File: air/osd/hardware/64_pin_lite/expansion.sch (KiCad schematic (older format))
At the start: 2 parts, among them P2 CONN_20, P3 CONN_20

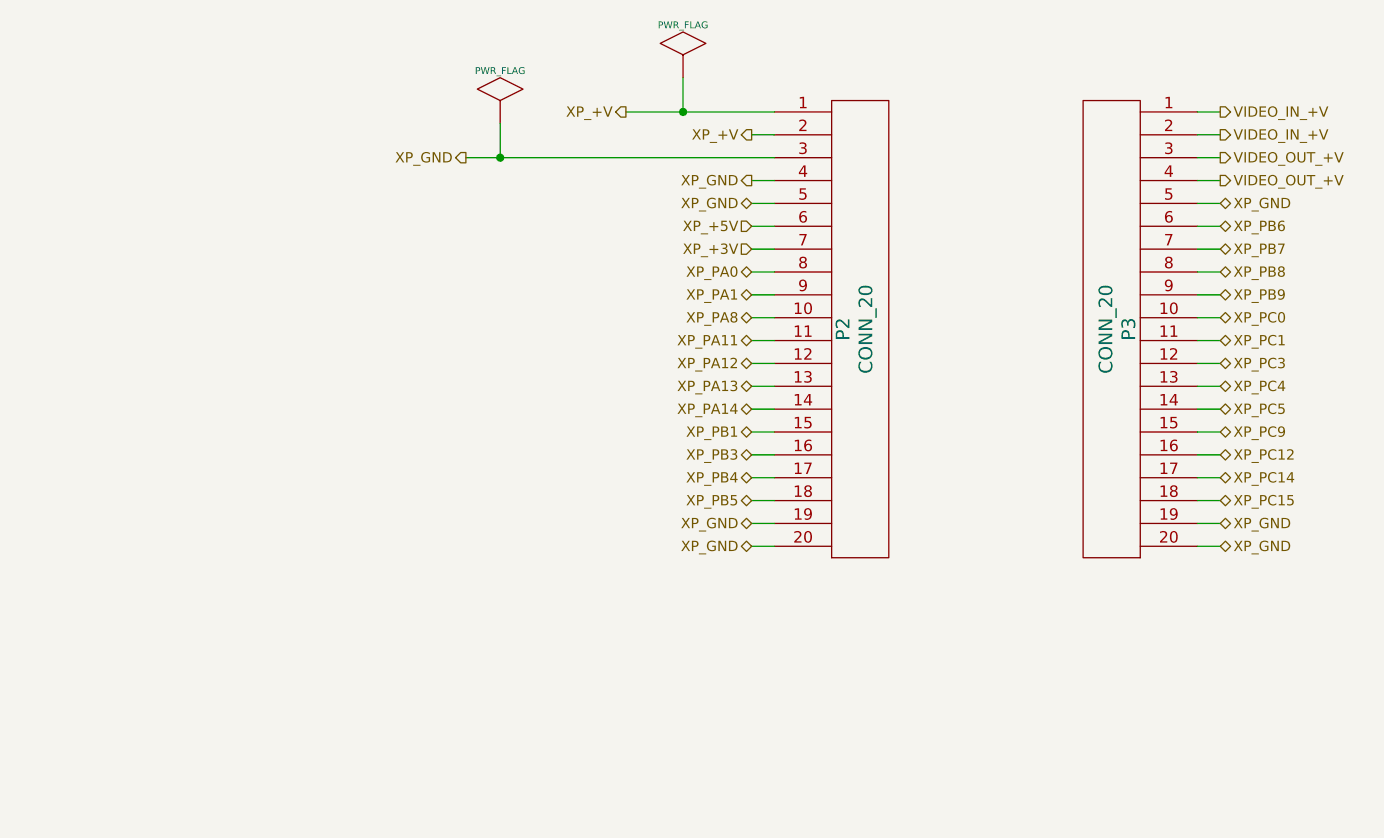
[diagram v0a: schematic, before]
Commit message: osd first  no eror routing of pcb
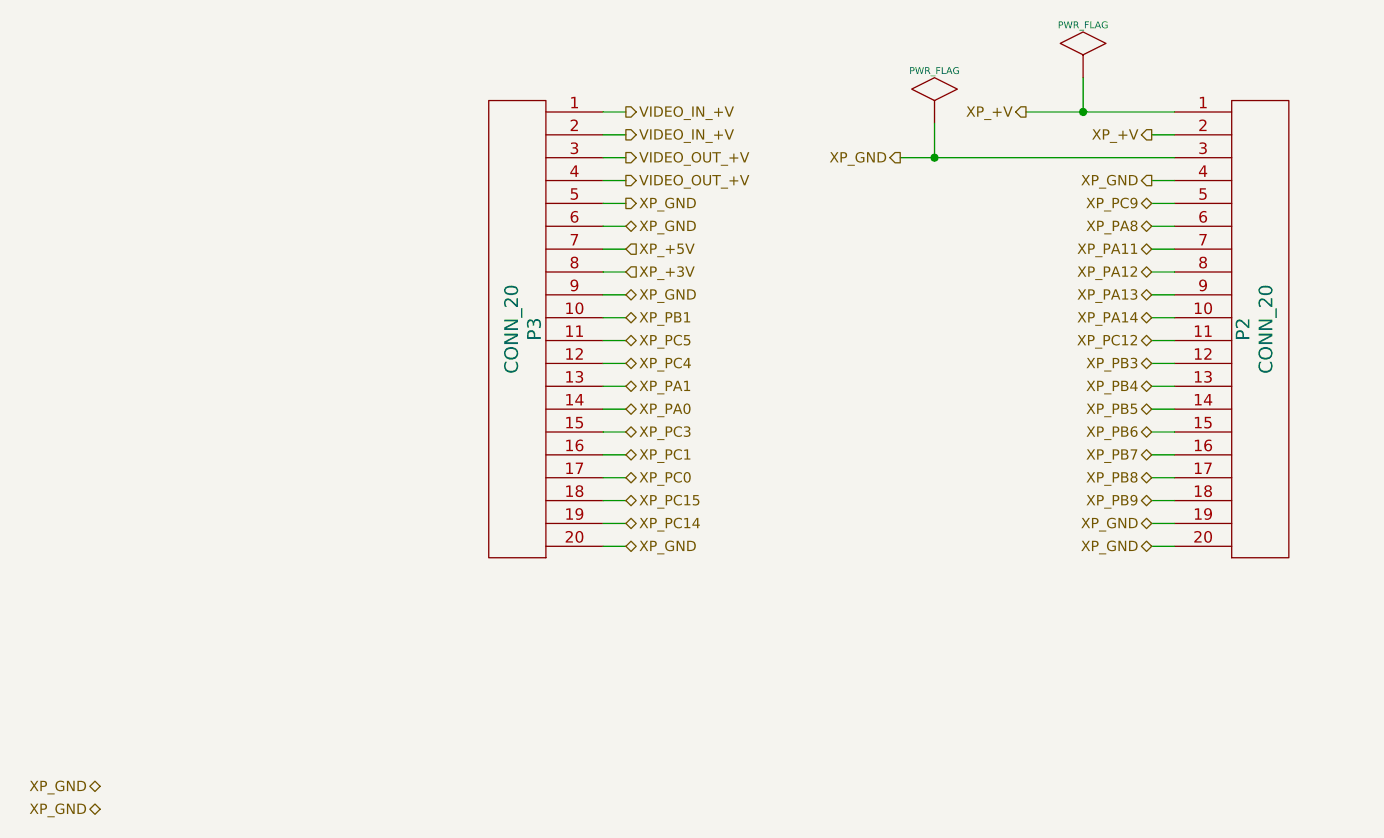
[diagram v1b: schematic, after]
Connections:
- net XP_+3V: now also P3.8 (P8); no longer P2.7 (P7)
- net XP_+5V: now also P3.7 (P7); no longer P2.6 (P6)
- net XP_GND: now also P3.6 (P6), P3.9 (P9); no longer P2.5 (P5), P3.19 (P19)
- net XP_PA0: now also P3.14 (P14); no longer P2.8 (P8)
- net XP_PA1: now also P3.13 (P13); no longer P2.9 (P9)
- net XP_PA11: now also P2.7 (P7); no longer P2.11 (P11)
- net XP_PA12: now also P2.8 (P8); no longer P2.12 (P12)
- net XP_PA13: now also P2.9 (P9); no longer P2.13 (P13)
- net XP_PA14: now also P2.10 (P10); no longer P2.14 (P14)
- net XP_PA8: now also P2.6 (P6); no longer P2.10 (P10)
- net XP_PB1: now also P3.10 (P10); no longer P2.15 (P15)
- net XP_PB3: now also P2.12 (P12); no longer P2.16 (P16)
- net XP_PB4: now also P2.13 (P13); no longer P2.17 (P17)
- net XP_PB5: now also P2.14 (P14); no longer P2.18 (P18)
- net XP_PB6: now also P2.15 (P15); no longer P3.6 (P6)
- net XP_PB7: now also P2.16 (P16); no longer P3.7 (P7)
- net XP_PB8: now also P2.17 (P17); no longer P3.8 (P8)
- net XP_PB9: now also P2.18 (P18); no longer P3.9 (P9)
- net XP_PC0: now also P3.17 (P17); no longer P3.10 (P10)
- net XP_PC1: now also P3.16 (P16); no longer P3.11 (P11)
- net XP_PC12: now also P2.11 (P11); no longer P3.16 (P16)
- net XP_PC14: now also P3.19 (P19); no longer P3.17 (P17)
- net XP_PC3: now also P3.15 (P15); no longer P3.12 (P12)
- net XP_PC4: now also P3.12 (P12); no longer P3.13 (P13)
- net XP_PC5: now also P3.11 (P11); no longer P3.14 (P14)
- net XP_PC9: now also P2.5 (P5); no longer P3.15 (P15)
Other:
- moved on the sheet: P2, P3
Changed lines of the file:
@@
-EESchema Schematic File Version 2  date Thu 27 Nov 2014 15:59:43 GMT
+EESchema Schematic File Version 2  date Sat 29 Nov 2014 10:43:44 GMT
 LIBS:power
 LIBS:device
@@
 Sheet 5 8
 Title ""
-Date "27 nov 2014"
+Date "29 nov 2014"
 Rev ""
 Comp ""
@@
 Comment4 ""
 $EndDescr
-Connection ~ 3650 2700
-Wire Wire Line
-	3650 2550 3650 2700
-Wire Wire Line
-	6700 2800 6800 2800
-Wire Wire Line
-	6700 2600 6800 2600
-Wire Wire Line
-	4200 2500 4850 2500
-Wire Wire Line
-	4850 2700 3500 2700
-Wire Wire Line
-	6800 4300 6700 4300
-Wire Wire Line
-	6700 4400 6800 4400
-Wire Wire Line
-	6700 4100 6800 4100
-Wire Wire Line
-	6700 3900 6800 3900
-Wire Wire Line
-	6700 3700 6800 3700
-Wire Wire Line
-	6700 3500 6800 3500
-Wire Wire Line
-	6700 3300 6800 3300
-Wire Wire Line
-	6700 3100 6800 3100
-Wire Wire Line
-	4850 4400 4750 4400
-Wire Wire Line
-	4850 4200 4750 4200
-Wire Wire Line
-	4850 4000 4750 4000
-Wire Wire Line
-	4850 3800 4750 3800
-Wire Wire Line
-	4850 3600 4750 3600
-Wire Wire Line
-	4850 3400 4750 3400
-Wire Wire Line
-	4850 3200 4750 3200
-Wire Wire Line
-	4850 3000 4750 3000
-Wire Wire Line
-	4850 2900 4750 2900
-Wire Wire Line
-	4850 3300 4750 3300
-Wire Wire Line
-	4850 3500 4750 3500
-Wire Wire Line
-	4850 3700 4750 3700
-Wire Wire Line
-	4850 3900 4750 3900
-Wire Wire Line
-	4850 4100 4750 4100
-Wire Wire Line
-	4850 4300 4750 4300
-Wire Wire Line
-	6700 2900 6800 2900
-Wire Wire Line
-	6700 3000 6800 3000
-Wire Wire Line
-	6700 3200 6800 3200
-Wire Wire Line
-	6700 3400 6800 3400
-Wire Wire Line
-	6700 3600 6800 3600
-Wire Wire Line
-	6700 3800 6800 3800
-Wire Wire Line
-	6700 4000 6800 4000
-Wire Wire Line
-	6700 4200 6800 4200
-Wire Wire Line
-	4850 3100 4750 3100
-Wire Wire Line
-	4850 2800 4750 2800
-Wire Wire Line
-	4850 2600 4750 2600
-Wire Wire Line
-	6700 2500 6800 2500
-Wire Wire Line
-	6700 2700 6800 2700
-Wire Wire Line
-	4450 2500 4450 2350
-Connection ~ 4450 2500
+Wire Wire Line
+	6500 4400 6600 4400
+Wire Wire Line
+	6500 4200 6600 4200
+Wire Wire Line
+	6500 4000 6600 4000
+Wire Wire Line
+	6500 3800 6600 3800
+Wire Wire Line
+	6500 3600 6600 3600
+Wire Wire Line
+	6500 3400 6600 3400
+Wire Wire Line
+	6500 3200 6600 3200
+Wire Wire Line
+	6500 3000 6600 3000
+Wire Wire Line
+	6500 2800 6600 2800
+Wire Wire Line
+	4100 4300 4200 4300
+Wire Wire Line
+	4100 4100 4200 4100
+Wire Wire Line
+	4100 3900 4200 3900
+Wire Wire Line
+	4100 3700 4200 3700
+Wire Wire Line
+	4100 3500 4200 3500
+Wire Wire Line
+	4100 3300 4200 3300
+Wire Wire Line
+	4100 3100 4200 3100
+Connection ~ 5550 2700
+Wire Wire Line
+	5550 2550 5550 2700
+Wire Wire Line
+	4100 2800 4200 2800
+Wire Wire Line
+	4100 2600 4200 2600
+Wire Wire Line
+	5950 2500 6200 2500
+Wire Wire Line
+	6200 2500 6600 2500
+Wire Wire Line
+	6600 2700 5550 2700
+Wire Wire Line
+	5550 2700 5400 2700
+Wire Wire Line
+	4100 2900 4200 2900
+Wire Wire Line
+	6600 2600 6500 2600
+Wire Wire Line
+	4100 2500 4200 2500
+Wire Wire Line
+	4100 2700 4200 2700
+Wire Wire Line
+	6200 2350 6200 2500
+Connection ~ 6200 2500
+Wire Wire Line
+	4100 3000 4200 3000
+Wire Wire Line
+	4100 3200 4200 3200
+Wire Wire Line
+	4100 3400 4200 3400
+Wire Wire Line
+	4100 3600 4200 3600
+Wire Wire Line
+	4100 3800 4200 3800
+Wire Wire Line
+	4100 4000 4200 4000
+Wire Wire Line
+	4100 4200 4200 4200
+Wire Wire Line
+	4100 4400 4200 4400
+Wire Wire Line
+	6500 2900 6600 2900
+Wire Wire Line
+	6500 3100 6600 3100
+Wire Wire Line
+	6500 3300 6600 3300
+Wire Wire Line
+	6500 3500 6600 3500
+Wire Wire Line
+	6500 3700 6600 3700
+Wire Wire Line
+	6500 3900 6600 3900
+Wire Wire Line
+	6500 4100 6600 4100
+Wire Wire Line
+	6500 4300 6600 4300
+Text HLabel 6500 4400 0    45   BiDi ~ 0
+XP_GND
+Text HLabel 6500 2800 0    45   Output ~ 0
+XP_GND
 $Comp
 L PWR_FLAG #FLG03
 U 1 1 5474845E
-P 3650 2550
-F 0 "#FLG03" H 3650 2820 30  0001 C CNN
-F 1 "PWR_FLAG" H 3650 2780 30  0000 C CNN
-	1    3650 2550
+P 5550 2550
+F 0 "#FLG03" H 5550 2820 30  0001 C CNN
+F 1 "PWR_FLAG" H 5550 2780 30  0000 C CNN
+	1    5550 2550
 	1    0    0    -1
 $EndComp
-Text HLabel 4750 2600 0    45   Output ~ 0
+Text HLabel 6500 2600 0    45   Output ~ 0
 XP_+V
 $Comp
 L PWR_FLAG #FLG04
 U 1 1 54748449
-P 4450 2350
-F 0 "#FLG04" H 4450 2620 30  0001 C CNN
-F 1 "PWR_FLAG" H 4450 2580 30  0000 C CNN
-	1    4450 2350
+P 6200 2350
+F 0 "#FLG04" H 6200 2620 30  0001 C CNN
+F 1 "PWR_FLAG" H 6200 2580 30  0000 C CNN
+	1    6200 2350
 	1    0    0    -1
 $EndComp
-Text HLabel 6800 4300 2    45   BiDi ~ 0
-XP_GND
-Text HLabel 6800 2800 2    45   Output ~ 0
+Text HLabel 6500 4200 0    45   BiDi ~ 0
+XP_PB9
+Text HLabel 4200 2800 2    45   Output ~ 0
 VIDEO_OUT_+V
-Text HLabel 6800 2600 2    45   Output ~ 0
+Text HLabel 4200 2600 2    45   Output ~ 0
 VIDEO_IN_+V
-Text HLabel 6800 2700 2    45   Output ~ 0
+Text HLabel 4200 2700 2    45   Output ~ 0
 VIDEO_OUT_+V
-Text HLabel 6800 2500 2    45   Output ~ 0
+Text HLabel 4200 2500 2    45   Output ~ 0
 VIDEO_IN_+V
-Text HLabel 3500 2700 0    45   Output ~ 0
-XP_GND
-Text HLabel 4750 2800 0    45   Output ~ 0
+Text HLabel 5400 2700 0    45   Output ~ 0
+XP_GND
+Text HLabel 4200 2900 2    45   Output ~ 0
 XP_GND
 $Comp
 L CONN_20 P3
 U 1 1 54746DE4
-P 6350 3450
-F 0 "P3" V 6300 3450 60  0000 C CNN
-F 1 "CONN_20" V 6400 3450 60  0000 C CNN
-	1    6350 3450
+P 3750 3450
+F 0 "P3" V 3700 3450 60  0000 C CNN
+F 1 "CONN_20" V 3800 3450 60  0000 C CNN
+	1    3750 3450
 	-1   0    0    -1
 $EndComp
@@
 L CONN_20 P2
 U 1 1 54746D91
-P 5200 3450
-F 0 "P2" V 5150 3450 60  0000 C CNN
-F 1 "CONN_20" V 5250 3450 60  0000 C CNN
-	1    5200 3450
+P 6950 3450
+F 0 "P2" V 6900 3450 60  0000 C CNN
+F 1 "CONN_20" V 7000 3450 60  0000 C CNN
+	1    6950 3450
 	1    0    0    -1
 $EndComp
-Text HLabel 4750 4400 0    45   BiDi ~ 0
-XP_GND
-Text HLabel 4200 2500 0    45   Output ~ 0
+Text HLabel 1900 5550 0    45   BiDi ~ 0
+XP_GND
+Text HLabel 5950 2500 0    45   Output ~ 0
 XP_+V
-Text HLabel 4750 3100 0    45   Input ~ 0
+Text HLabel 4200 3200 2    45   Input ~ 0
 XP_+3V
-Text HLabel 6800 4400 2    45   BiDi ~ 0
-XP_GND
-Text HLabel 4750 4300 0    45   BiDi ~ 0
-XP_GND
-Text HLabel 6800 4200 2    45   BiDi ~ 0
+Text HLabel 6500 4300 0    45   BiDi ~ 0
+XP_GND
+Text HLabel 1900 5450 0    45   BiDi ~ 0
+XP_GND
+Text HLabel 6500 4100 0    45   BiDi ~ 0
+XP_PB8
+Text HLabel 6500 4000 0    45   BiDi ~ 0
+XP_PB7
+Text HLabel 6500 3800 0    45   BiDi ~ 0
+XP_PB5
+Text HLabel 6500 3700 0    45   BiDi ~ 0
+XP_PB4
+Text HLabel 6500 3600 0    45   BiDi ~ 0
+XP_PB3
+Text HLabel 6500 3500 0    45   BiDi ~ 0
+XP_PC12
+Text HLabel 6500 3400 0    45   BiDi ~ 0
+XP_PA14
+Text HLabel 6500 3300 0    45   BiDi ~ 0
+XP_PA13
+Text HLabel 6500 3900 0    45   BiDi ~ 0
+XP_PB6
+Text HLabel 6500 3200 0    45   BiDi ~ 0
+XP_PA12
+Text HLabel 6500 3100 0    45   BiDi ~ 0
+XP_PA11
+Text HLabel 6500 3000 0    45   BiDi ~ 0
+XP_PA8
+Text HLabel 6500 2900 0    45   BiDi ~ 0
+XP_PC9
+Text HLabel 4200 4300 2    45   BiDi ~ 0
+XP_PC14
+Text HLabel 4200 4200 2    45   BiDi ~ 0
 XP_PC15
-Text HLabel 6800 4100 2    45   BiDi ~ 0
-XP_PC14
-Text HLabel 6800 3900 2    45   BiDi ~ 0
-XP_PC9
-Text HLabel 6800 3800 2    45   BiDi ~ 0
+Text HLabel 4200 4100 2    45   BiDi ~ 0
+XP_PC0
+Text HLabel 4200 4000 2    45   BiDi ~ 0
+XP_PC1
+Text HLabel 4200 3900 2    45   BiDi ~ 0
+XP_PC3
+Text HLabel 4200 3800 2    45   BiDi ~ 0
+XP_PA0
+Text HLabel 4200 3700 2    45   BiDi ~ 0
+XP_PA1
+Text HLabel 4200 3600 2    45   BiDi ~ 0
+XP_PC4
+Text HLabel 4200 3500 2    45   BiDi ~ 0
 XP_PC5
-Text HLabel 6800 3700 2    45   BiDi ~ 0
-XP_PC4
-Text HLabel 6800 3600 2    45   BiDi ~ 0
-XP_PC3
-Text HLabel 6800 3500 2    45   BiDi ~ 0
-XP_PC1
-Text HLabel 6800 3400 2    45   BiDi ~ 0
-XP_PC0
-Text HLabel 6800 4000 2    45   BiDi ~ 0
-XP_PC12
-Text HLabel 6800 3300 2    45   BiDi ~ 0
-XP_PB9
-Text HLabel 6800 3200 2    45   BiDi ~ 0
-XP_PB8
-Text HLabel 6800 3100 2    45   BiDi ~ 0
-XP_PB7
-Text HLabel 6800 3000 2    45   BiDi ~ 0
-XP_PB6
-Text HLabel 4750 4200 0    45   BiDi ~ 0
-XP_PB5
-Text HLabel 4750 4100 0    45   BiDi ~ 0
-XP_PB4
-Text HLabel 4750 4000 0    45   BiDi ~ 0
-XP_PB3
-Text HLabel 4750 3900 0    45   BiDi ~ 0
+Text HLabel 4200 3400 2    45   BiDi ~ 0
 XP_PB1
-Text HLabel 4750 3800 0    45   BiDi ~ 0
-XP_PA14
-Text HLabel 4750 3700 0    45   BiDi ~ 0
-XP_PA13
-Text HLabel 4750 3600 0    45   BiDi ~ 0
-XP_PA12
-Text HLabel 4750 3500 0    45   BiDi ~ 0
-XP_PA11
-Text HLabel 4750 3400 0    45   BiDi ~ 0
-XP_PA8
-Text HLabel 4750 3300 0    45   BiDi ~ 0
-XP_PA1
-Text HLabel 4750 3200 0    45   BiDi ~ 0
-XP_PA0
-Text HLabel 4750 3000 0    45   Input ~ 0
+Text HLabel 4200 3300 2    45   BiDi ~ 0
+XP_GND
+Text HLabel 4200 3100 2    45   Input ~ 0
 XP_+5V
-Text HLabel 6800 2900 2    45   BiDi ~ 0
-XP_GND
-Text HLabel 4750 2900 0    45   BiDi ~ 0
+Text HLabel 4200 4400 2    45   BiDi ~ 0
+XP_GND
+Text HLabel 4200 3000 2    45   BiDi ~ 0
 XP_GND
 $EndSCHEMATC

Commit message: osd tidying and added reset to header connector
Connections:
- net XP_GND: no longer P2.19 (P19)
- new net XP_NRST: P2.19 (P19)
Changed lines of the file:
@@
-EESchema Schematic File Version 2  date Sat 29 Nov 2014 10:43:44 GMT
+EESchema Schematic File Version 2  date Sun 30 Nov 2014 15:34:12 GMT
 LIBS:power
 LIBS:device
@@
 Sheet 5 8
 Title ""
-Date "29 nov 2014"
+Date "30 nov 2014"
 Rev ""
 Comp ""
@@
 	4100 2600 4200 2600
 Wire Wire Line
-	5950 2500 6200 2500
-Wire Wire Line
-	6200 2500 6600 2500
-Wire Wire Line
-	6600 2700 5550 2700
-Wire Wire Line
-	5550 2700 5400 2700
+	5950 2500 6600 2500
+Wire Wire Line
+	6600 2700 5400 2700
 Wire Wire Line
 	4100 2900 4200 2900
@@
 Text HLabel 4200 3200 2    45   Input ~ 0
 XP_+3V
-Text HLabel 6500 4300 0    45   BiDi ~ 0
-XP_GND
+Text HLabel 6500 4300 0    45   Output ~ 0
+XP_NRST
 Text HLabel 1900 5450 0    45   BiDi ~ 0
 XP_GND

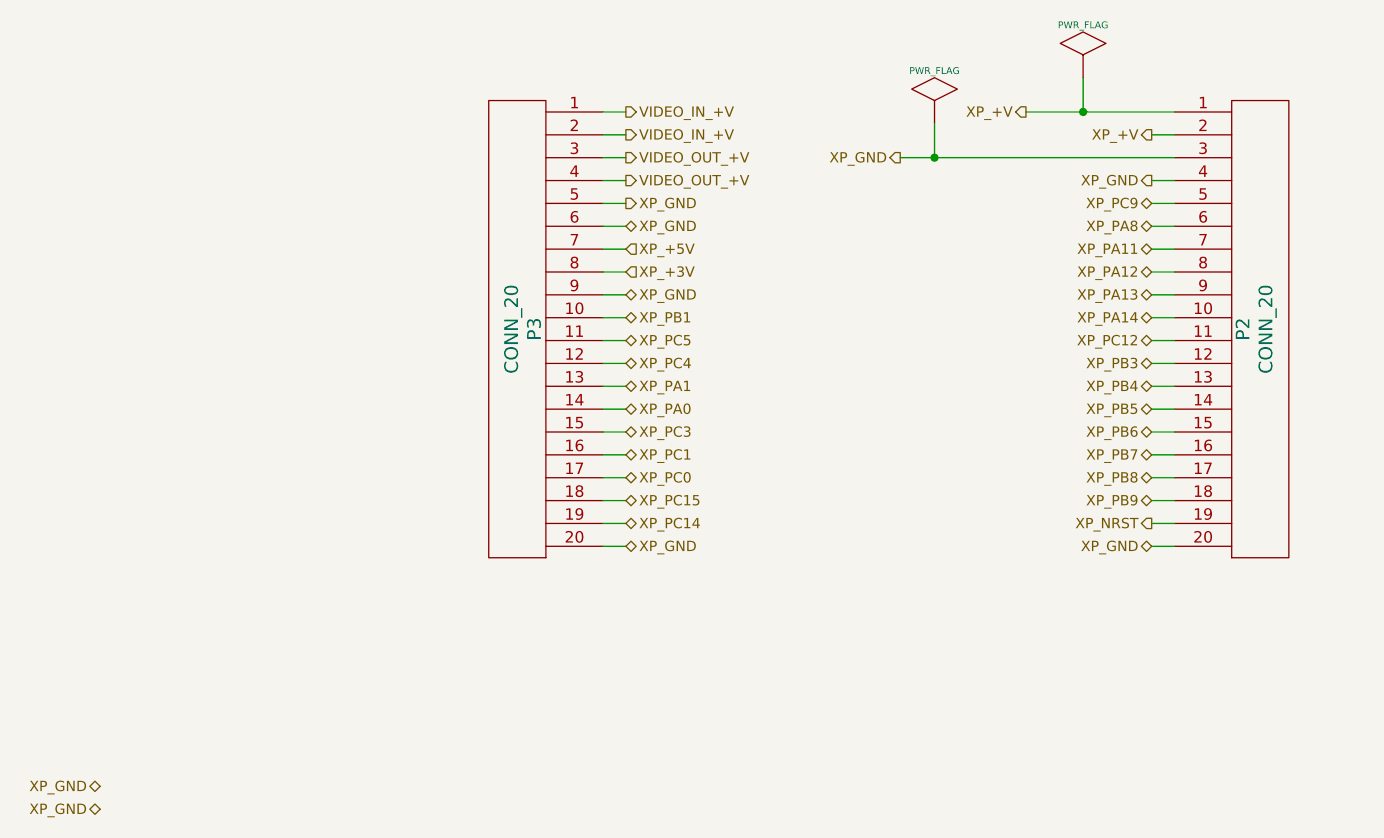
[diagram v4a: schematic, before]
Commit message: on pcb added battery level resistor divider. On code compiled and built ok but not uploaded or tested
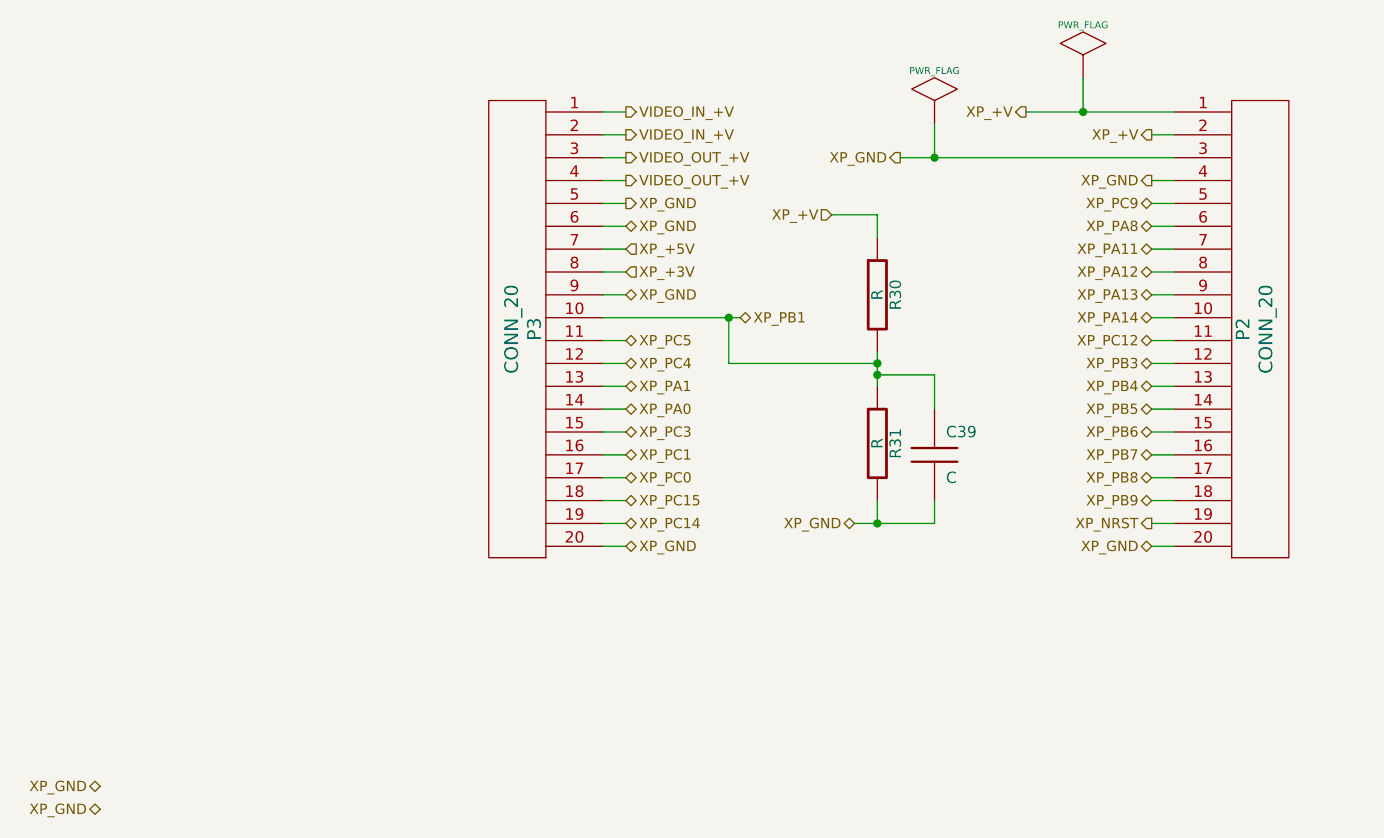
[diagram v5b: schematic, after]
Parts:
- added C39: C, symbol C
- added R30, R31: R, symbol R
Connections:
- net XP_+V: now also R30.1
- net XP_GND: now also C39.2, R31.2
- net XP_PB1: now also C39.1, R30.2, R31.1
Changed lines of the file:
@@
-EESchema Schematic File Version 2  date Tue 02 Dec 2014 12:33:05 GMT
+EESchema Schematic File Version 2  date Wed 03 Dec 2014 09:37:23 GMT
 LIBS:power
 LIBS:device
@@
 Sheet 5 8
 Title ""
-Date "2 dec 2014"
+Date "3 dec 2014"
 Rev ""
 Comp ""
@@
 Comment4 ""
 $EndDescr
+Connection ~ 4650 3400
+Wire Wire Line
+	4650 3400 4650 3600
+Connection ~ 5300 3600
+Wire Wire Line
+	4650 3600 5300 3600
+Connection ~ 5300 3650
+Wire Wire Line
+	5550 3800 5550 3650
+Wire Wire Line
+	5550 3650 5300 3650
+Wire Wire Line
+	5300 3050 5300 2950
+Wire Wire Line
+	5300 2950 5100 2950
 Wire Wire Line
 	6500 4400 6600 4400
@@
 	4100 3200 4200 3200
 Wire Wire Line
-	4100 3400 4200 3400
+	4100 3400 4700 3400
 Wire Wire Line
 	4100 3600 4200 3600
@@
 Wire Wire Line
 	6500 4300 6600 4300
+Wire Wire Line
+	5300 3700 5300 3550
+Wire Wire Line
+	5300 4200 5300 4300
+Wire Wire Line
+	5200 4300 5550 4300
+Wire Wire Line
+	5550 4300 5550 4200
+Connection ~ 5300 4300
+$Comp
+L C C39
+U 1 1 547ED333
+P 5550 4000
+F 0 "C39" H 5600 4100 50  0000 L CNN
+F 1 "C" H 5600 3900 50  0000 L CNN
+	1    5550 4000
+	1    0    0    -1
+$EndComp
+Text HLabel 5100 2950 0    45   Input ~ 0
+XP_+V
+Text HLabel 5200 4300 0    45   BiDi ~ 0
+XP_GND
+$Comp
+L R R31
+U 1 1 547ED2AB
+P 5300 3950
+F 0 "R31" V 5380 3950 50  0000 C CNN
+F 1 "R" V 5300 3950 50  0000 C CNN
+	1    5300 3950
+	1    0    0    -1
+$EndComp
+$Comp
+L R R30
+U 1 1 547ED2A5
+P 5300 3300
+F 0 "R30" V 5380 3300 50  0000 C CNN
+F 1 "R" V 5300 3300 50  0000 C CNN
+	1    5300 3300
+	1    0    0    -1
+$EndComp
 Text HLabel 6500 4400 0    45   BiDi ~ 0
 XP_GND
@@
 Text HLabel 4200 3500 2    45   BiDi ~ 0
 XP_PC5
-Text HLabel 4200 3400 2    45   BiDi ~ 0
+Text HLabel 4700 3400 2    45   BiDi ~ 0
 XP_PB1
 Text HLabel 4200 3300 2    45   BiDi ~ 0
